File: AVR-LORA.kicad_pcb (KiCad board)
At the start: 2 copper layers, 47 x 29.2 mm, 36 parts, among them J1 Batt, J2 Solar, J3 CONN_01X01, J4 CONN_01X14, J5 CONN_01X14, U1 MCP1700-3302E_SOT23, U2 RFM95HW, U3 AVR128DB28, Y1 24MHz, Y2 32768Hz

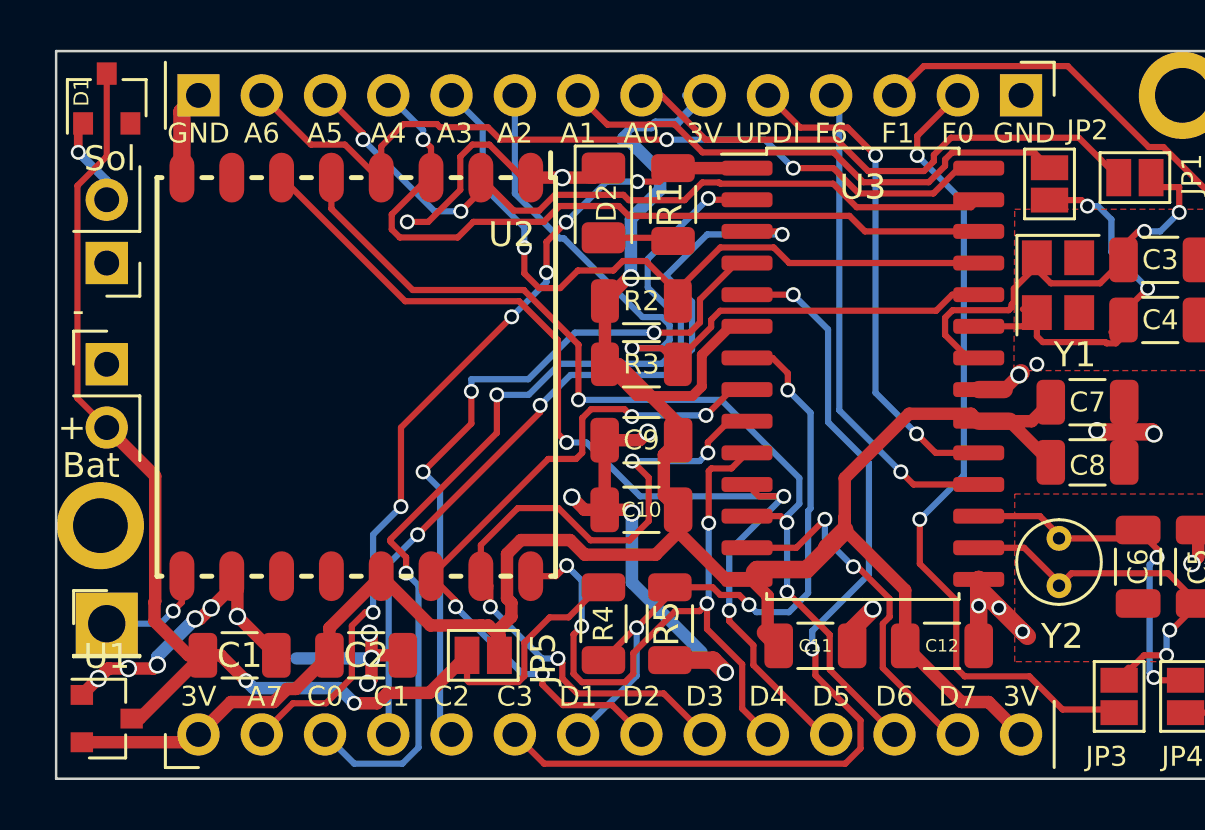
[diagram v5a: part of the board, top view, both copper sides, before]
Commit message: Add PDF and PNG to AVR
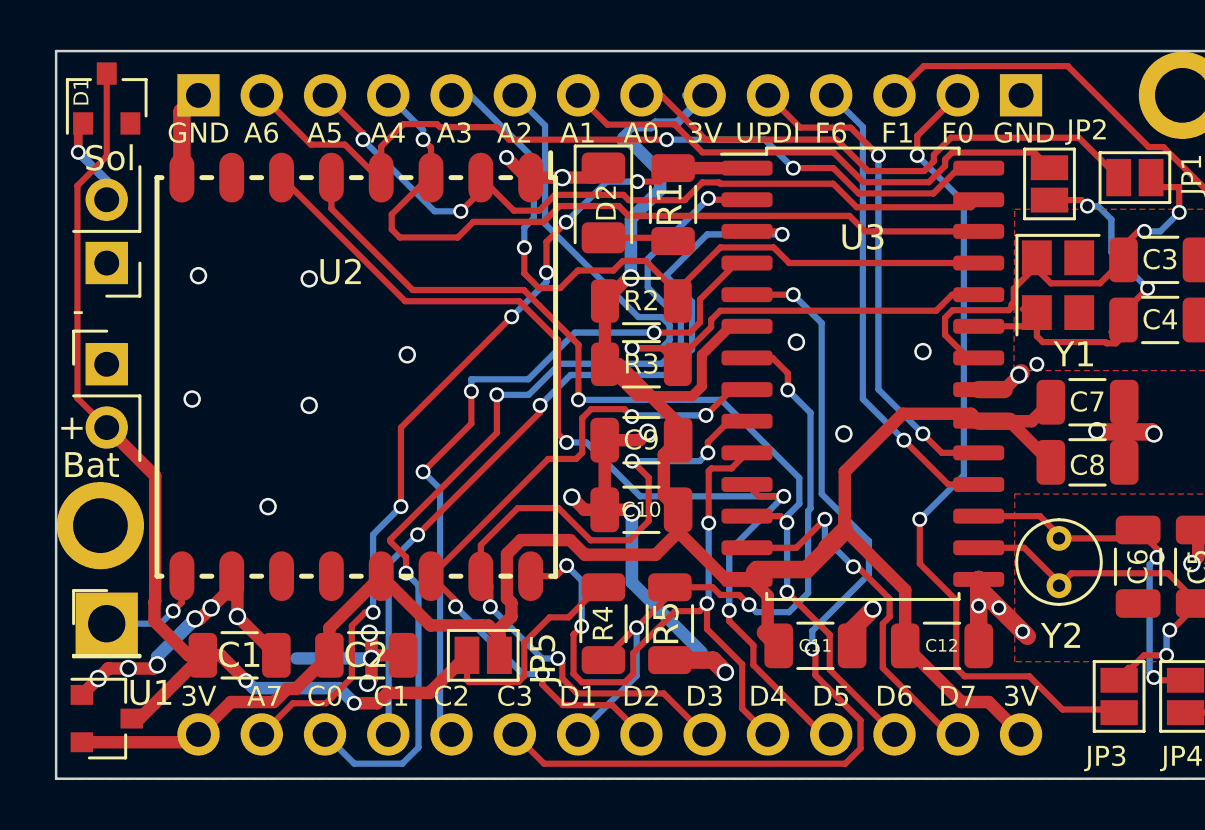
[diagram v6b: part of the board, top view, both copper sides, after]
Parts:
- J4, J5: moved to B.Cu
- turned J4 to 270 degrees
- turned J5 to 90 degrees
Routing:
- net GND: track 67.6 -> 61.7 mm, vias 24 -> 33
- net /F6: track 19.6 -> 18.8 mm
- net /A3: track 29.8 -> 30.5 mm
- removed copper zone on F.Cu, net /3V3

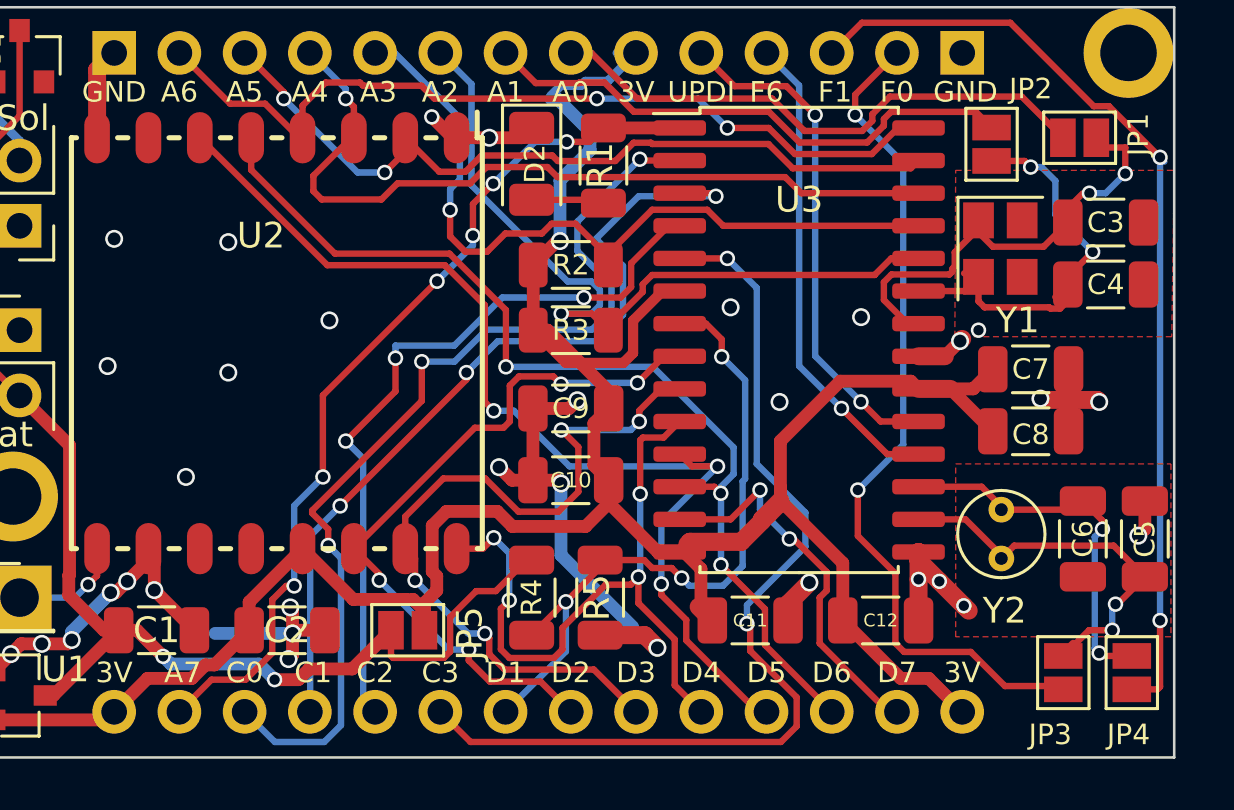
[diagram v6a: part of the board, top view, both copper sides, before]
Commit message: Update 32768 config and PDF and PNG for AVR
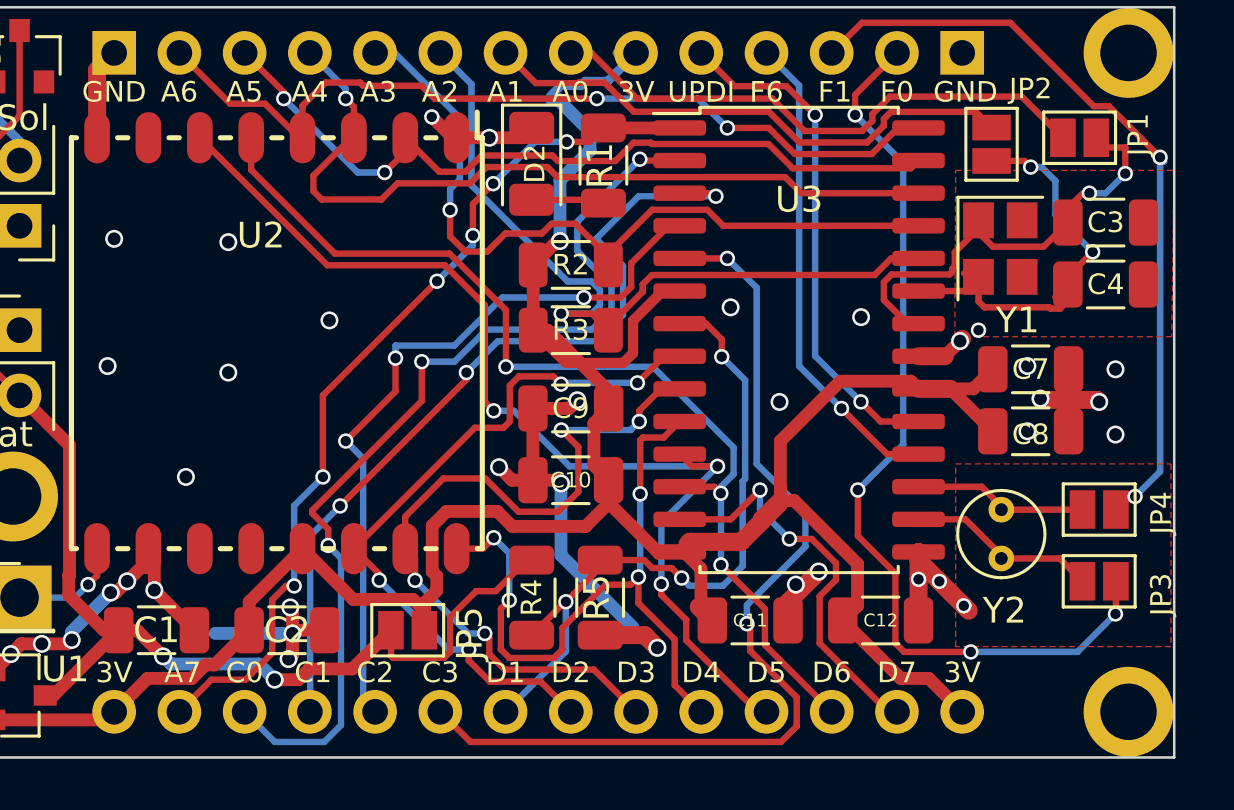
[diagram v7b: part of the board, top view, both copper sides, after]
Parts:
- removed C5, C6: 12pF, Capacitor_SMD:C_1206_3216Metric
- added REF**: MountingHole_2.2mm_M2_ISO7380_Pad, MountingHole:MountingHole_2.2mm_M2_ISO7380_Pad, F.Cu at (117.5, 109.1)
- moved JP4 6.48 mm to (116.3, 101.2), turned to 0 degrees
- moved JP3 3.82 mm to (116.3, 104.0), turned to 0 degrees
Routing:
- net /F0: track 16.0 -> 7.51 mm, vias 2 -> 0
- net /F1: track 14.8 -> 6.88 mm, vias 2 -> 0
- net /CF1: track 37.4 -> 30.2 mm
- net /CF0: track 33.0 -> 36.4 mm, vias 2 -> 4
- net GND: track 61.7 -> 60.8 mm, vias 33 -> 37
- net /3V3: track 112.5 -> 113.2 mm
- net /D7: track 15.0 -> 15.7 mm

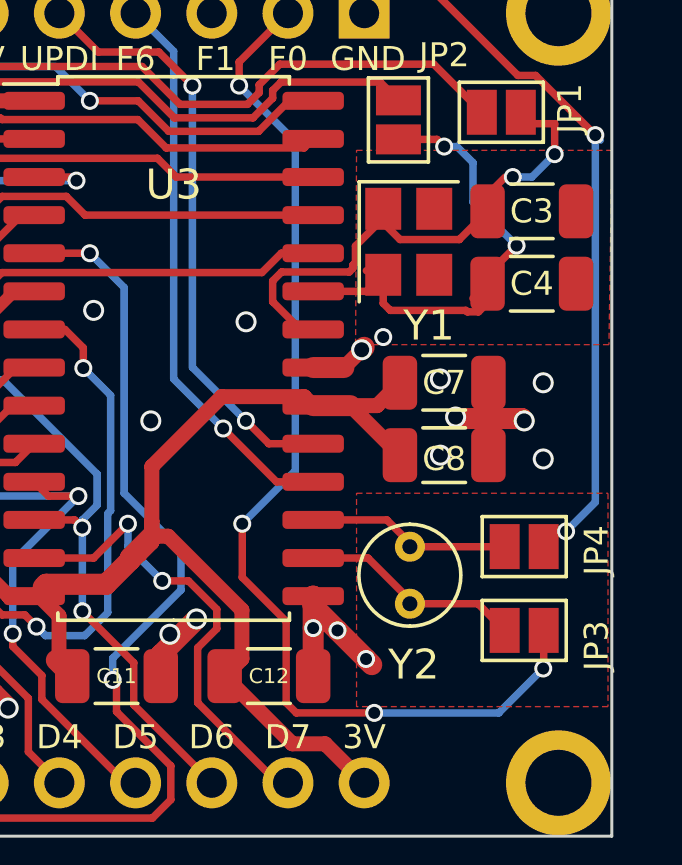
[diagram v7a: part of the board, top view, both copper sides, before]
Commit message: Update 24MHz crystal config and PDF and PNG for AVR
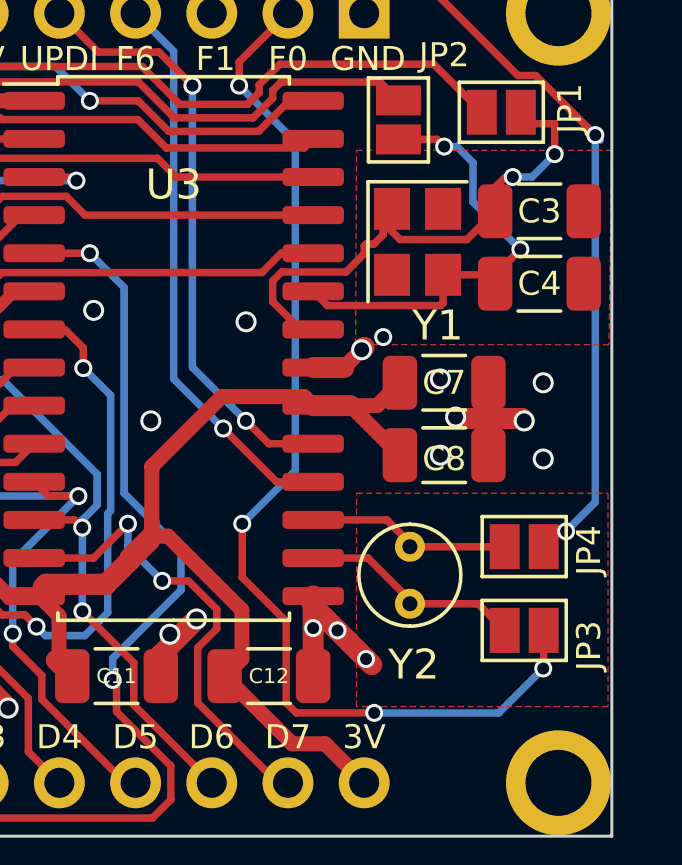
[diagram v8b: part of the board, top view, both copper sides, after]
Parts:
- moved Y1 0.29 mm to (112.8, 91.1)
- moved C3 0.25 mm to (116.8, 90.0)
- moved C4 0.25 mm to (116.8, 92.5)
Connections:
- Y1 pad 2: /A1 -> Net-(Y1-Pad2)
- Y1 pad 3: (no net) -> /A1
- Y1 pad 4: (no net) -> Net-(Y1-Pad4)
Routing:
- net /A1: track 17.2 -> 15.6 mm
